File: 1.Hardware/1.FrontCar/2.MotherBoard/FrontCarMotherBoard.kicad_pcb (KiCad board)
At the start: 2 copper layers, 72 parts, among them IC1 SN74LVC244APW, J1 2YGP2Y0A02, J10 MOTOR, J11 MOTOR, J12 Maple, J13 SERVO, J14 IO, J15 IO, J16 IO, J17 IO, J18 Conn_02x05_Odd_Even, J2 AUX, J4 TOF, J5 L_ENCODER, J6 WIRELESS, J8 R_ENCODER, J9 ELEMAG, Q1 S8050, SW2 SW_5DIR, SW3 SW_SPDT, U3 LM2940S-5.0, U4 RT9013-33GB, U5 SCEP, U6 MT9V034

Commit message: 母板基本设计完成
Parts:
- added ?: , , F.Cu at (202.1, 80.4)
- added ?: , , F.Cu at (139.3, 21.2)
- added ?: , , F.Cu at (94.1, 80.4)
- D5: footprint Diode_SMD:D_SOD-123 -> Diode_SMD:D_SMA
- moved C15 344.9 mm to (128.6, 39.9), turned to -90 degrees
- moved C10 341.7 mm to (130.9, 39.9), turned to 90 degrees
- moved 9013 340.1 mm to (136.6, 39.7), turned to 180 degrees
- moved C9 338.8 mm to (133.0, 39.9), turned to 90 degrees
- moved CAM 338.1 mm to (136.0, 48.8)
- moved R? 337.4 mm to (109.2, 41.9), turned to 180 degrees
- moved R5 336.2 mm to (136.1, 46.8)
- moved Q1 332.6 mm to (109.1, 44.9), turned to 180 degrees
- moved BZ1 326.0 mm to (113.5, 52.8), turned to 180 degrees
- moved G 322.8 mm to (169.1, 27.5)
- moved CAM 316.8 mm to (173.6, 27.5)
- moved SW2 311.9 mm to (100.0, 52.8)
- moved 3V3 310.9 mm to (178.2, 27.5)
- moved TP? 305.0 mm to (182.7, 27.5)
- moved IC1 299.6 mm to (131.6, 29.8), turned to 180 degrees
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- renumbered U3 to 2940, J1 to 2YGP, TP3 to 3V3, J17 to 3V3, D4 to 5V, J15 to 5V, TP1 to 6V, D2 to 6V, U4 to 9013, J2 to AUX, J6 to BLE, D3 to CAM, TP4 to CAM, J16 to G, TP5 to G, J14 to J13, J9 to J8, J5 to L_ENC, J12 to MAPLE, J11 to MOTOR, J8 to R_ENC, J13 to SERVO, SW3 to SW1, J18 to SWD, J4 to TOF
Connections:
- 2940 pad 4: GND -> GNDPWR
- 9013 pad 2: GNDPWR -> GND
- C10 pad 2: GNDPWR -> GND
- C15 pad 2: GNDPWR -> GND
- C9 pad 2: GNDPWR -> GND
- CAM pad 1: GNDPWR -> GND
- J10 pad 1: /Ports/MOTOR_PWR -> GNDPWR
- J10 pad 2: GNDPWR -> /Ports/MOTOR_PWR
- J? pad 1: VBUS -> GNDPWR
- J? pad 2: GNDPWR -> VBUS
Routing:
- net /Coreboard/5V: track 0.00 -> 247.2 mm, vias 0 -> 2
- net /Peripheral/3V3: track 0.00 -> 227.8 mm, vias 0 -> 1
- net /Ports/MOTOR_PWR: track 0.00 -> 157.6 mm
- net GNDPWR: track 0.00 -> 114.3 mm
- net /Coreboard/BATTERY: track 0.00 -> 92.3 mm, vias 0 -> 2
- net /Coreboard/MOTORL_PWM: track 0.00 -> 89.7 mm, vias 0 -> 1
- net /Coreboard/MOTORR_PWM: track 0.00 -> 85.9 mm, vias 0 -> 1
- net /Coreboard/MOTORL_DIR: track 0.00 -> 79.7 mm, vias 0 -> 1
- net /Coreboard/MOTORR_DIR: track 0.00 -> 77.2 mm, vias 0 -> 1
- net VCC: track 0.00 -> 76.2 mm
- net /Coreboard/AUX_SCL: track 0.00 -> 69.5 mm, vias 0 -> 1
- net /Ports/SERVO_6V: track 0.00 -> 68.2 mm
- net /Coreboard/SWCLK: track 0.00 -> 65.4 mm
- net /Peripheral/CAM_3V3: track 0.00 -> 63.6 mm, vias 0 -> 2
- net /Coreboard/AUX_SDA: track 0.00 -> 62.7 mm, vias 0 -> 1
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- added copper zone on F.Cu, net /Coreboard/5V
- added copper zone on F.Cu, net /Peripheral/CAM_3V3
- added copper zone on F.Cu, net /Ports/MOTOR_PWR
- added copper zone on B.Cu, net GND
- added copper zone on F.Cu, net GND
- added copper zone on B.Cu, net GNDPWR
- added copper zone on F.Cu, net GNDPWR
- added copper zone on B.Cu, net VBUS
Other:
- board outline added: 134.6 x 100.2 mm
- board text added: "A0"
- board text added: "A1"
- board text added: "A15"
- board text added: "A2"
- board text added: "A3"
- board text added: "A4"
- board text added: "A5"
- board text added: "A6"
- board text added: "A7"
- board text added: "B4"
- board text added: "B5"
- board text added: "C3"
- board text added: "C4"
- board text added: "CL"
- board text added: "D13"
- board text added: "D14"
- board text added: "DA"
- board text added: "F6"
- board text added: "F7"
- board text added: "G"
- board text added: "G10"
- board text added: "G11"
- board text added: "G12"
- board text added: "G13"
- board text added: "G14"
- board text added: "G9"
- board text added: "ON OFF"
- board text added: "V"

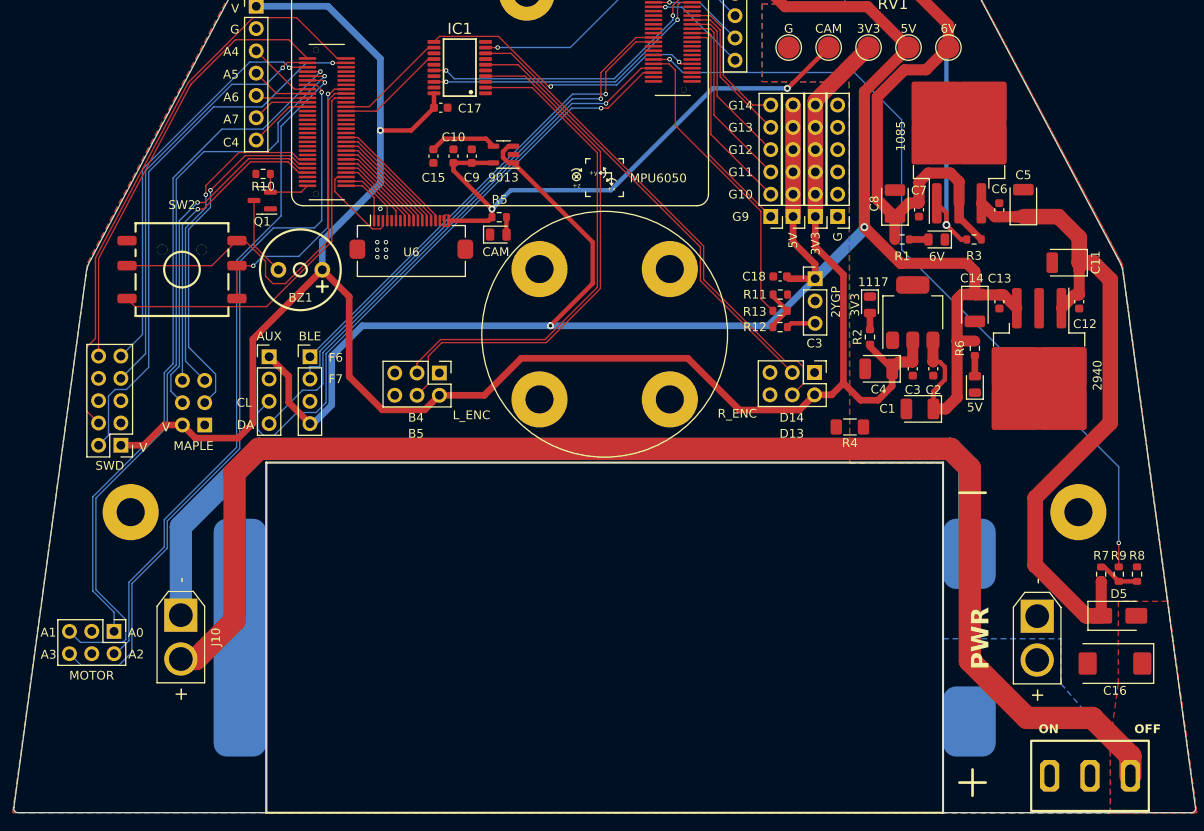
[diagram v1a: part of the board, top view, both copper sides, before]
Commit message: 母板增加丝印
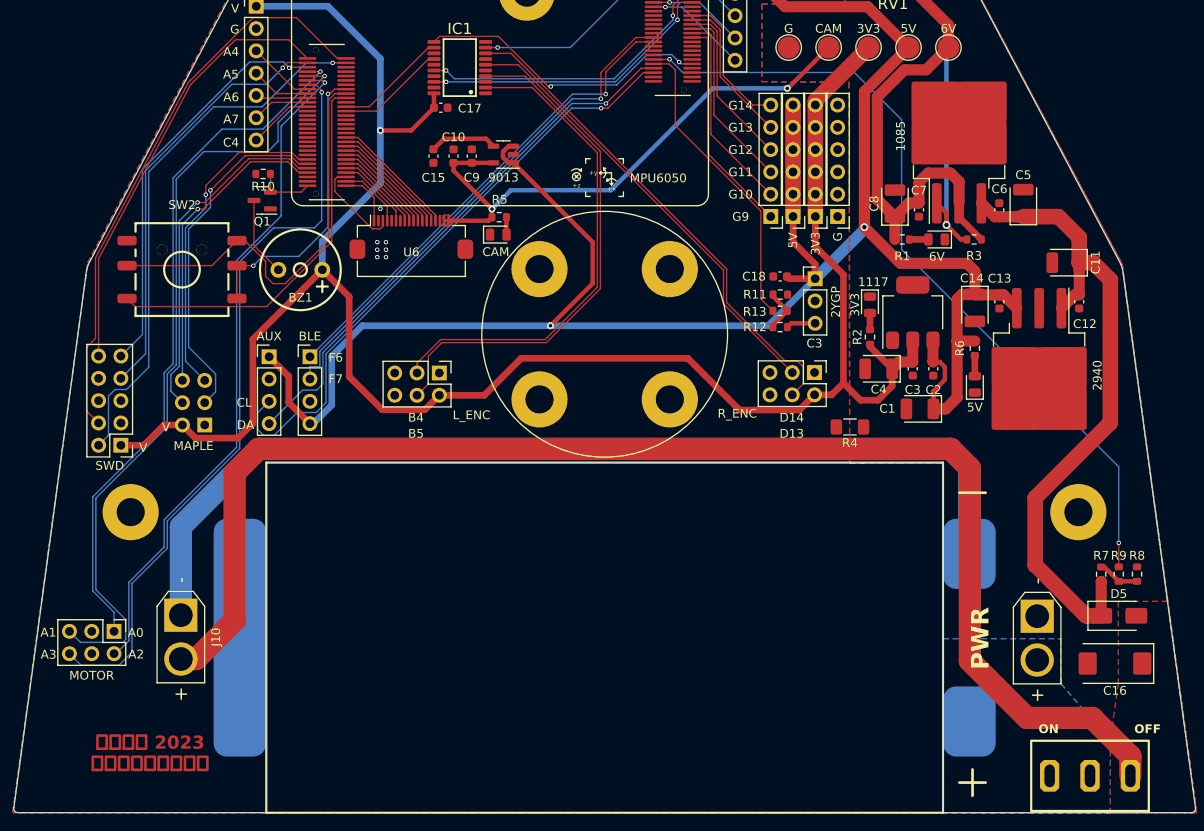
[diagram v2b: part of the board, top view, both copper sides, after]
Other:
- board text added: "东华大学 2023 有人把我队名抢了队"
